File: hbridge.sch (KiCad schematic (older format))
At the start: 17 parts

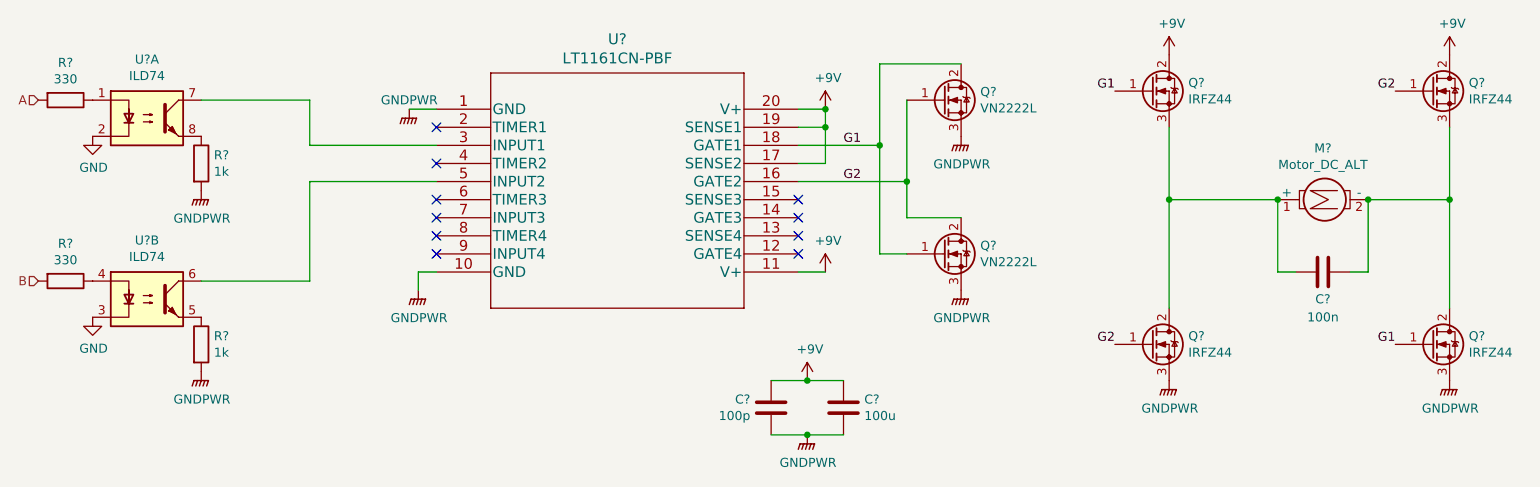
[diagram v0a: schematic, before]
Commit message: Add part numbers
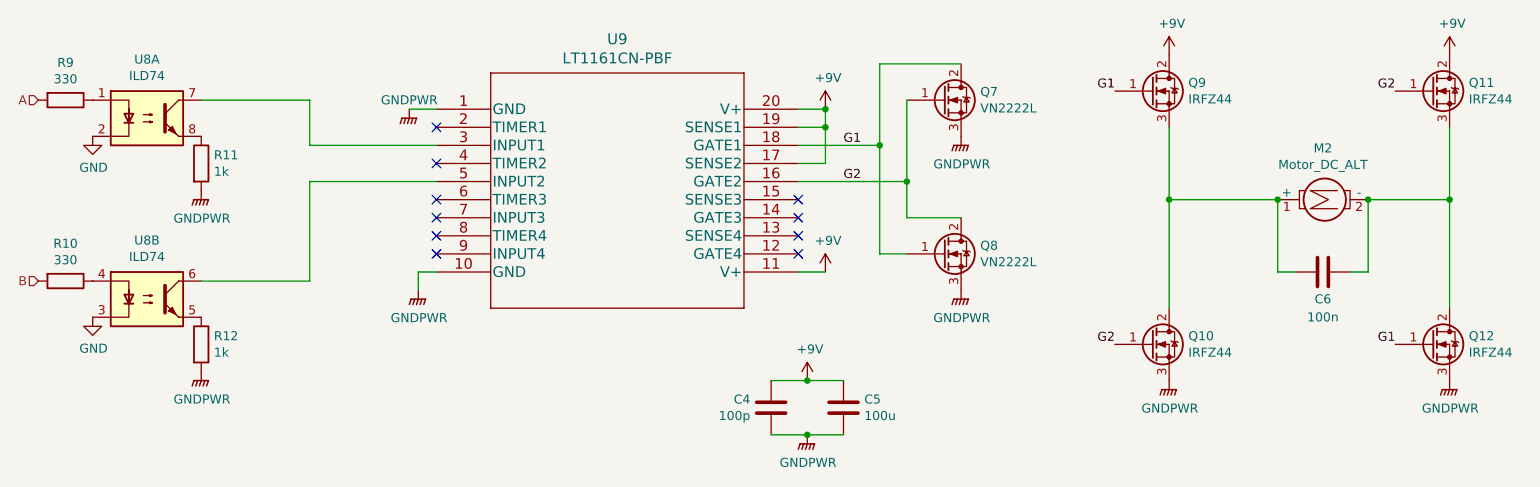
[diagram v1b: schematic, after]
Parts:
- gave numbers to parts that had none: 16
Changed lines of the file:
@@
 $EndDescr
 $Comp
-L Motor:Motor_DC_ALT M?
+L Motor:Motor_DC_ALT M1
 U 1 1 5EFAE763
 P 9000 3500
-AR Path="/5EFA9D4F/5EFAE763" Ref="M?"  Part="1"
-AR Path="/5F04487B/5EFAE763" Ref="M?"  Part="1"
-F 0 "M?" V 8716 3450 50  0000 C CNN
+AR Path="/5EFA9D4F/5EFAE763" Ref="M1"  Part="1"
+AR Path="/5F04487B/5EFAE763" Ref="M2"  Part="1"
+F 0 "M2" V 8716 3450 50  0000 C CNN
 F 1 "Motor_DC_ALT" V 8807 3450 50  0000 C CNN
 F 2 "" H 9000 3410 50  0001 C CNN
@@
 	9300 3900 9300 3500
 $Comp
-L Isolator:ILD74 U?
+L Isolator:ILD74 U6
 U 1 1 5EFB4C9B
 P 2550 3050
-AR Path="/5EFA9D4F/5EFB4C9B" Ref="U?"  Part="1"
-AR Path="/5F04487B/5EFB4C9B" Ref="U?"  Part="1"
-F 0 "U?" H 2550 3375 50  0000 C CNN
+AR Path="/5EFA9D4F/5EFB4C9B" Ref="U6"  Part="1"
+AR Path="/5F04487B/5EFB4C9B" Ref="U8"  Part="1"
+F 0 "U8" H 2550 3375 50  0000 C CNN
 F 1 "ILD74" H 2550 3284 50  0000 C CNN
 F 2 "" H 2350 2850 50  0001 L CIN
@@
 $EndComp
 $Comp
-L Isolator:ILD74 U?
+L Isolator:ILD74 U6
 U 2 1 5EFB57BF
 P 2550 4050
-AR Path="/5EFA9D4F/5EFB57BF" Ref="U?"  Part="2"
-AR Path="/5F04487B/5EFB57BF" Ref="U?"  Part="2"
-F 0 "U?" H 2550 4375 50  0000 C CNN
+AR Path="/5EFA9D4F/5EFB57BF" Ref="U6"  Part="2"
+AR Path="/5F04487B/5EFB57BF" Ref="U8"  Part="2"
+F 0 "U8" H 2550 4375 50  0000 C CNN
 F 1 "ILD74" H 2550 4284 50  0000 C CNN
 F 2 "" H 2350 3850 50  0001 L CIN
@@
 $EndComp
 $Comp
-L Device:R R?
+L Device:R R8
 U 1 1 5EFB6EDB
 P 2850 4300
-AR Path="/5EFA9D4F/5EFB6EDB" Ref="R?"  Part="1"
-AR Path="/5F04487B/5EFB6EDB" Ref="R?"  Part="1"
-F 0 "R?" H 2920 4346 50  0000 L CNN
+AR Path="/5EFA9D4F/5EFB6EDB" Ref="R8"  Part="1"
+AR Path="/5F04487B/5EFB6EDB" Ref="R12"  Part="1"
+F 0 "R12" H 2920 4346 50  0000 L CNN
 F 1 "1k" H 2920 4255 50  0000 L CNN
 F 2 "" V 2780 4300 50  0001 C CNN
@@
 $EndComp
 $Comp
-L Device:R R?
+L Device:R R7
 U 1 1 5EFB7506
 P 2850 3300
-AR Path="/5EFA9D4F/5EFB7506" Ref="R?"  Part="1"
-AR Path="/5F04487B/5EFB7506" Ref="R?"  Part="1"
-F 0 "R?" H 2920 3346 50  0000 L CNN
+AR Path="/5EFA9D4F/5EFB7506" Ref="R7"  Part="1"
+AR Path="/5F04487B/5EFB7506" Ref="R11"  Part="1"
+F 0 "R11" H 2920 3346 50  0000 L CNN
 F 1 "1k" H 2920 3255 50  0000 L CNN
 F 2 "" V 2780 3300 50  0001 C CNN
@@
 $EndComp
 $Comp
-L Device:R R?
+L Device:R R5
 U 1 1 5EFB9D51
 P 2100 2950
-AR Path="/5EFA9D4F/5EFB9D51" Ref="R?"  Part="1"
-AR Path="/5F04487B/5EFB9D51" Ref="R?"  Part="1"
-F 0 "R?" V 1893 2950 50  0000 C CNN
+AR Path="/5EFA9D4F/5EFB9D51" Ref="R5"  Part="1"
+AR Path="/5F04487B/5EFB9D51" Ref="R9"  Part="1"
+F 0 "R9" V 1893 2950 50  0000 C CNN
 F 1 "330" V 1984 2950 50  0000 C CNN
 F 2 "" V 2030 2950 50  0001 C CNN
@@
 $EndComp
 $Comp
-L Device:R R?
+L Device:R R6
 U 1 1 5EFBA4CA
 P 2100 3950
-AR Path="/5EFA9D4F/5EFBA4CA" Ref="R?"  Part="1"
-AR Path="/5F04487B/5EFBA4CA" Ref="R?"  Part="1"
-F 0 "R?" V 1893 3950 50  0000 C CNN
+AR Path="/5EFA9D4F/5EFBA4CA" Ref="R6"  Part="1"
+AR Path="/5F04487B/5EFBA4CA" Ref="R10"  Part="1"
+F 0 "R10" V 1893 3950 50  0000 C CNN
 F 1 "330" V 1984 3950 50  0000 C CNN
 F 2 "" V 2030 3950 50  0001 C CNN
@@
 $EndComp
 $Comp
-L Device:C C?
+L Device:C C1
 U 1 1 5EFBBB55
 P 6000 4650
-AR Path="/5EFA9D4F/5EFBBB55" Ref="C?"  Part="1"
-AR Path="/5F04487B/5EFBBB55" Ref="C?"  Part="1"
-F 0 "C?" H 5885 4604 50  0000 R CNN
+AR Path="/5EFA9D4F/5EFBBB55" Ref="C1"  Part="1"
+AR Path="/5F04487B/5EFBBB55" Ref="C4"  Part="1"
+F 0 "C4" H 5885 4604 50  0000 R CNN
 F 1 "100p" H 5885 4695 50  0000 R CNN
 F 2 "" H 6038 4500 50  0001 C CNN
@@
 $EndComp
 $Comp
-L Device:C C?
+L Device:C C2
 U 1 1 5EFBC147
 P 6400 4650
-AR Path="/5EFA9D4F/5EFBC147" Ref="C?"  Part="1"
-AR Path="/5F04487B/5EFBC147" Ref="C?"  Part="1"
-F 0 "C?" H 6515 4696 50  0000 L CNN
+AR Path="/5EFA9D4F/5EFBC147" Ref="C2"  Part="1"
+AR Path="/5F04487B/5EFBC147" Ref="C5"  Part="1"
+F 0 "C5" H 6515 4696 50  0000 L CNN
 F 1 "100u" H 6515 4605 50  0000 L CNN
 F 2 "" H 6438 4500 50  0001 C CNN
@@
 $EndComp
 $Comp
-L Device:Q_NMOS_GDS Q?
+L Device:Q_NMOS_GDS Q1
 U 1 1 5EFE7548
 P 6950 2950
-AR Path="/5EFA9D4F/5EFE7548" Ref="Q?"  Part="1"
-AR Path="/5F04487B/5EFE7548" Ref="Q?"  Part="1"
-F 0 "Q?" H 7156 2996 50  0000 L CNN
+AR Path="/5EFA9D4F/5EFE7548" Ref="Q1"  Part="1"
+AR Path="/5F04487B/5EFE7548" Ref="Q7"  Part="1"
+F 0 "Q7" H 7156 2996 50  0000 L CNN
 F 1 "VN2222L" H 7156 2905 50  0000 L CNN
 F 2 "" H 7150 3050 50  0001 C CNN
@@
 $EndComp
 $Comp
-L Device:Q_NMOS_GDS Q?
+L Device:Q_NMOS_GDS Q2
 U 1 1 5EFE9639
 P 6950 3800
-AR Path="/5EFA9D4F/5EFE9639" Ref="Q?"  Part="1"
-AR Path="/5F04487B/5EFE9639" Ref="Q?"  Part="1"
-F 0 "Q?" H 7156 3846 50  0000 L CNN
+AR Path="/5EFA9D4F/5EFE9639" Ref="Q2"  Part="1"
+AR Path="/5F04487B/5EFE9639" Ref="Q8"  Part="1"
+F 0 "Q8" H 7156 3846 50  0000 L CNN
 F 1 "VN2222L" H 7156 3755 50  0000 L CNN
 F 2 "" H 7150 3900 50  0001 C CNN
@@
 $EndComp
 $Comp
-L Device:Q_NMOS_GDS Q?
+L Device:Q_NMOS_GDS Q3
 U 1 1 5EFE9DB0
 P 8100 2900
-AR Path="/5EFA9D4F/5EFE9DB0" Ref="Q?"  Part="1"
-AR Path="/5F04487B/5EFE9DB0" Ref="Q?"  Part="1"
-F 0 "Q?" H 8306 2946 50  0000 L CNN
+AR Path="/5EFA9D4F/5EFE9DB0" Ref="Q3"  Part="1"
+AR Path="/5F04487B/5EFE9DB0" Ref="Q9"  Part="1"
+F 0 "Q9" H 8306 2946 50  0000 L CNN
 F 1 "IRFZ44" H 8306 2855 50  0000 L CNN
 F 2 "" H 8300 3000 50  0001 C CNN
@@
 $EndComp
 $Comp
-L Device:Q_NMOS_GDS Q?
+L Device:Q_NMOS_GDS Q4
 U 1 1 5EFEA31E
 P 8100 4300
-AR Path="/5EFA9D4F/5EFEA31E" Ref="Q?"  Part="1"
-AR Path="/5F04487B/5EFEA31E" Ref="Q?"  Part="1"
-F 0 "Q?" H 8306 4346 50  0000 L CNN
+AR Path="/5EFA9D4F/5EFEA31E" Ref="Q4"  Part="1"
+AR Path="/5F04487B/5EFEA31E" Ref="Q10"  Part="1"
+F 0 "Q10" H 8306 4346 50  0000 L CNN
 F 1 "IRFZ44" H 8306 4255 50  0000 L CNN
 F 2 "" H 8300 4400 50  0001 C CNN
@@
 $EndComp
 $Comp
-L Device:Q_NMOS_GDS Q?
+L Device:Q_NMOS_GDS Q5
 U 1 1 5EFEB4E2
 P 9650 2900
-AR Path="/5EFA9D4F/5EFEB4E2" Ref="Q?"  Part="1"
-AR Path="/5F04487B/5EFEB4E2" Ref="Q?"  Part="1"
-F 0 "Q?" H 9856 2946 50  0000 L CNN
+AR Path="/5EFA9D4F/5EFEB4E2" Ref="Q5"  Part="1"
+AR Path="/5F04487B/5EFEB4E2" Ref="Q11"  Part="1"
+F 0 "Q11" H 9856 2946 50  0000 L CNN
 F 1 "IRFZ44" H 9856 2855 50  0000 L CNN
 F 2 "" H 9850 3000 50  0001 C CNN
@@
 $EndComp
 $Comp
-L Device:Q_NMOS_GDS Q?
+L Device:Q_NMOS_GDS Q6
 U 1 1 5EFEB900
 P 9650 4300
-AR Path="/5EFA9D4F/5EFEB900" Ref="Q?"  Part="1"
-AR Path="/5F04487B/5EFEB900" Ref="Q?"  Part="1"
-F 0 "Q?" H 9856 4346 50  0000 L CNN
+AR Path="/5EFA9D4F/5EFEB900" Ref="Q6"  Part="1"
+AR Path="/5F04487B/5EFEB900" Ref="Q12"  Part="1"
+F 0 "Q12" H 9856 4346 50  0000 L CNN
 F 1 "IRFZ44" H 9856 4255 50  0000 L CNN
 F 2 "" H 9850 4400 50  0001 C CNN
@@
 	8900 3900 8800 3900
 $Comp
-L Device:C C?
+L Device:C C3
 U 1 1 5EFAF223
 P 9050 3900
-AR Path="/5EFA9D4F/5EFAF223" Ref="C?"  Part="1"
-AR Path="/5F04487B/5EFAF223" Ref="C?"  Part="1"
-F 0 "C?" V 9200 3900 50  0000 C CNN
+AR Path="/5EFA9D4F/5EFAF223" Ref="C3"  Part="1"
+AR Path="/5F04487B/5EFAF223" Ref="C6"  Part="1"
+F 0 "C6" V 9200 3900 50  0000 C CNN
 F 1 "100n" V 9300 3900 50  0000 C CNN
 F 2 "" H 9088 3750 50  0001 C CNN
@@
 $EndComp
 $Comp
-L LT1161CNPBF:LT1161CN-PBF U?
+L LT1161CNPBF:LT1161CN-PBF U7
 U 1 1 5EFCF468
 P 4150 3000
-AR Path="/5EFA9D4F/5EFCF468" Ref="U?"  Part="1"
-AR Path="/5F04487B/5EFCF468" Ref="U?"  Part="1"
-F 0 "U?" H 5150 3387 60  0000 C CNN
+AR Path="/5EFA9D4F/5EFCF468" Ref="U7"  Part="1"
+AR Path="/5F04487B/5EFCF468" Ref="U9"  Part="1"
+F 0 "U9" H 5150 3387 60  0000 C CNN
 F 1 "LT1161CN-PBF" H 5150 3281 60  0000 C CNN
 F 2 "PDIP-20_N_LIT" H 5150 3240 60  0001 C CNN

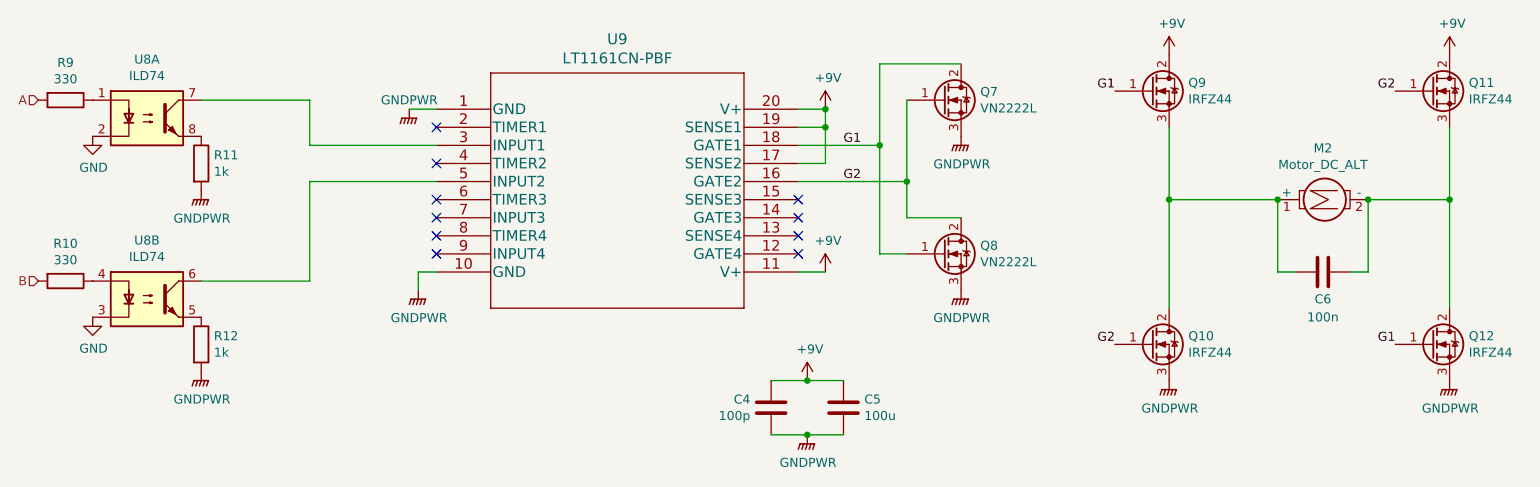
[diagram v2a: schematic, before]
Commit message: Add debug panel
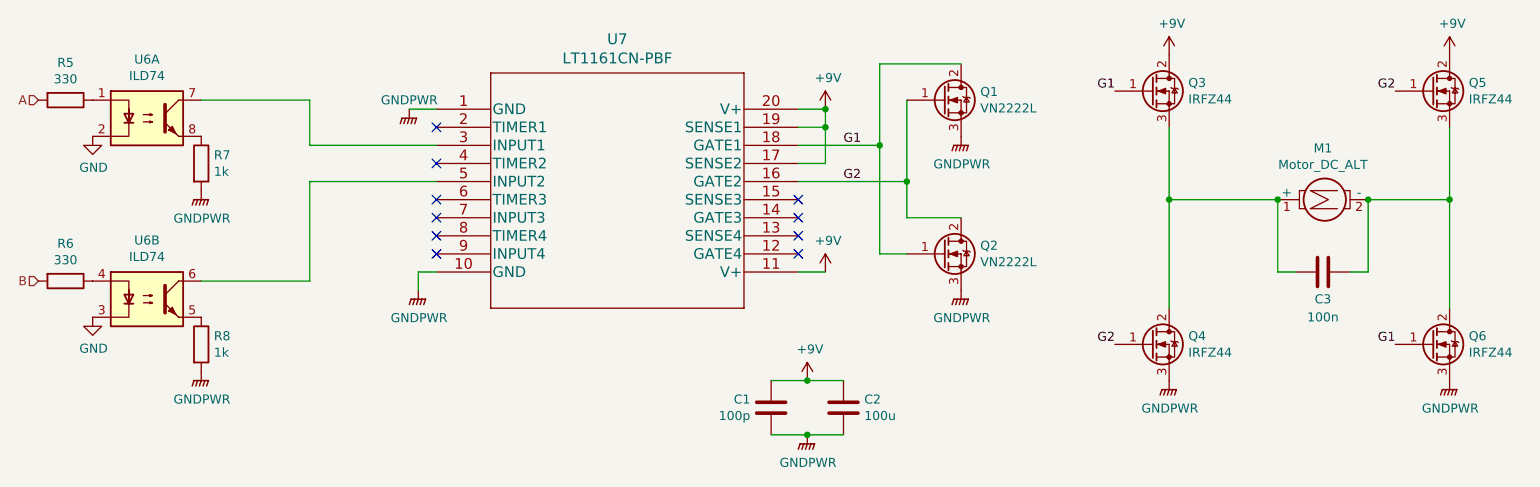
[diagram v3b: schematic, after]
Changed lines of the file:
@@
 $Descr A4 11693 8268
 encoding utf-8
-Sheet 2 3
+Sheet 2 6
 Title ""
 Date ""
@@
 AR Path="/5EFA9D4F/5EFAE763" Ref="M1"  Part="1"
 AR Path="/5F04487B/5EFAE763" Ref="M2"  Part="1"
-F 0 "M2" V 8716 3450 50  0000 C CNN
+F 0 "M1" V 8716 3450 50  0000 C CNN
 F 1 "Motor_DC_ALT" V 8807 3450 50  0000 C CNN
 F 2 "" H 9000 3410 50  0001 C CNN
@@
 AR Path="/5EFA9D4F/5EFB4C9B" Ref="U6"  Part="1"
 AR Path="/5F04487B/5EFB4C9B" Ref="U8"  Part="1"
-F 0 "U8" H 2550 3375 50  0000 C CNN
+F 0 "U6" H 2550 3375 50  0000 C CNN
 F 1 "ILD74" H 2550 3284 50  0000 C CNN
 F 2 "" H 2350 2850 50  0001 L CIN
@@
 AR Path="/5EFA9D4F/5EFB57BF" Ref="U6"  Part="2"
 AR Path="/5F04487B/5EFB57BF" Ref="U8"  Part="2"
-F 0 "U8" H 2550 4375 50  0000 C CNN
+F 0 "U6" H 2550 4375 50  0000 C CNN
 F 1 "ILD74" H 2550 4284 50  0000 C CNN
 F 2 "" H 2350 3850 50  0001 L CIN
@@
 AR Path="/5EFA9D4F/5EFB6EDB" Ref="R8"  Part="1"
 AR Path="/5F04487B/5EFB6EDB" Ref="R12"  Part="1"
-F 0 "R12" H 2920 4346 50  0000 L CNN
+F 0 "R8" H 2920 4346 50  0000 L CNN
 F 1 "1k" H 2920 4255 50  0000 L CNN
 F 2 "" V 2780 4300 50  0001 C CNN
@@
 AR Path="/5EFA9D4F/5EFB7506" Ref="R7"  Part="1"
 AR Path="/5F04487B/5EFB7506" Ref="R11"  Part="1"
-F 0 "R11" H 2920 3346 50  0000 L CNN
+F 0 "R7" H 2920 3346 50  0000 L CNN
 F 1 "1k" H 2920 3255 50  0000 L CNN
 F 2 "" V 2780 3300 50  0001 C CNN
@@
 AR Path="/5EFA9D4F/5EFB9D51" Ref="R5"  Part="1"
 AR Path="/5F04487B/5EFB9D51" Ref="R9"  Part="1"
-F 0 "R9" V 1893 2950 50  0000 C CNN
+F 0 "R5" V 1893 2950 50  0000 C CNN
 F 1 "330" V 1984 2950 50  0000 C CNN
 F 2 "" V 2030 2950 50  0001 C CNN
@@
 AR Path="/5EFA9D4F/5EFBA4CA" Ref="R6"  Part="1"
 AR Path="/5F04487B/5EFBA4CA" Ref="R10"  Part="1"
-F 0 "R10" V 1893 3950 50  0000 C CNN
+F 0 "R6" V 1893 3950 50  0000 C CNN
 F 1 "330" V 1984 3950 50  0000 C CNN
 F 2 "" V 2030 3950 50  0001 C CNN
@@
 AR Path="/5EFA9D4F/5EFBBB55" Ref="C1"  Part="1"
 AR Path="/5F04487B/5EFBBB55" Ref="C4"  Part="1"
-F 0 "C4" H 5885 4604 50  0000 R CNN
+F 0 "C1" H 5885 4604 50  0000 R CNN
 F 1 "100p" H 5885 4695 50  0000 R CNN
 F 2 "" H 6038 4500 50  0001 C CNN
@@
 AR Path="/5EFA9D4F/5EFBC147" Ref="C2"  Part="1"
 AR Path="/5F04487B/5EFBC147" Ref="C5"  Part="1"
-F 0 "C5" H 6515 4696 50  0000 L CNN
+F 0 "C2" H 6515 4696 50  0000 L CNN
 F 1 "100u" H 6515 4605 50  0000 L CNN
 F 2 "" H 6438 4500 50  0001 C CNN
@@
 AR Path="/5EFA9D4F/5EFE7548" Ref="Q1"  Part="1"
 AR Path="/5F04487B/5EFE7548" Ref="Q7"  Part="1"
-F 0 "Q7" H 7156 2996 50  0000 L CNN
+F 0 "Q1" H 7156 2996 50  0000 L CNN
 F 1 "VN2222L" H 7156 2905 50  0000 L CNN
 F 2 "" H 7150 3050 50  0001 C CNN
@@
 AR Path="/5EFA9D4F/5EFE9639" Ref="Q2"  Part="1"
 AR Path="/5F04487B/5EFE9639" Ref="Q8"  Part="1"
-F 0 "Q8" H 7156 3846 50  0000 L CNN
+F 0 "Q2" H 7156 3846 50  0000 L CNN
 F 1 "VN2222L" H 7156 3755 50  0000 L CNN
 F 2 "" H 7150 3900 50  0001 C CNN
@@
 AR Path="/5EFA9D4F/5EFE9DB0" Ref="Q3"  Part="1"
 AR Path="/5F04487B/5EFE9DB0" Ref="Q9"  Part="1"
-F 0 "Q9" H 8306 2946 50  0000 L CNN
+F 0 "Q3" H 8306 2946 50  0000 L CNN
 F 1 "IRFZ44" H 8306 2855 50  0000 L CNN
 F 2 "" H 8300 3000 50  0001 C CNN
@@
 AR Path="/5EFA9D4F/5EFEA31E" Ref="Q4"  Part="1"
 AR Path="/5F04487B/5EFEA31E" Ref="Q10"  Part="1"
-F 0 "Q10" H 8306 4346 50  0000 L CNN
+F 0 "Q4" H 8306 4346 50  0000 L CNN
 F 1 "IRFZ44" H 8306 4255 50  0000 L CNN
 F 2 "" H 8300 4400 50  0001 C CNN
@@
 AR Path="/5EFA9D4F/5EFEB4E2" Ref="Q5"  Part="1"
 AR Path="/5F04487B/5EFEB4E2" Ref="Q11"  Part="1"
-F 0 "Q11" H 9856 2946 50  0000 L CNN
+F 0 "Q5" H 9856 2946 50  0000 L CNN
 F 1 "IRFZ44" H 9856 2855 50  0000 L CNN
 F 2 "" H 9850 3000 50  0001 C CNN
@@
 AR Path="/5EFA9D4F/5EFEB900" Ref="Q6"  Part="1"
 AR Path="/5F04487B/5EFEB900" Ref="Q12"  Part="1"
-F 0 "Q12" H 9856 4346 50  0000 L CNN
+F 0 "Q6" H 9856 4346 50  0000 L CNN
 F 1 "IRFZ44" H 9856 4255 50  0000 L CNN
 F 2 "" H 9850 4400 50  0001 C CNN
@@
 AR Path="/5EFA9D4F/5EFAF223" Ref="C3"  Part="1"
 AR Path="/5F04487B/5EFAF223" Ref="C6"  Part="1"
-F 0 "C6" V 9200 3900 50  0000 C CNN
+F 0 "C3" V 9200 3900 50  0000 C CNN
 F 1 "100n" V 9300 3900 50  0000 C CNN
 F 2 "" H 9088 3750 50  0001 C CNN
@@
 AR Path="/5EFA9D4F/5EFCF468" Ref="U7"  Part="1"
 AR Path="/5F04487B/5EFCF468" Ref="U9"  Part="1"
-F 0 "U9" H 5150 3387 60  0000 C CNN
+F 0 "U7" H 5150 3387 60  0000 C CNN
 F 1 "LT1161CN-PBF" H 5150 3281 60  0000 C CNN
 F 2 "PDIP-20_N_LIT" H 5150 3240 60  0001 C CNN
